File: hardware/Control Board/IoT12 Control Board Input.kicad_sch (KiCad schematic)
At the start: 28 parts, among them SW1 Rotary encoder EC11 Plum 15mm, U2 ADS1115IDGS, U3 INA826AID, U4 INA826AID

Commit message: Start of next iteration.
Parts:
- removed J1, J2: ~, TestPoint:TestPoint_THTPad_D2.0mm_Drill1.0mm, symbol Connector_Generic:Conn_01x01
- removed SW1: Rotary encoder EC11 Plum 15mm, Rotary_Encoder-fixed:RotaryEncoder_Alps_EC11E-Switch_Vertical_H20mm_CircularMountingHoles, symbol Device:RotaryEncoder_Switch
- added J6: JST B6B-XH-A, Connector_JST:JST_XH_B6B-XH-A_1x06_P2.50mm_Vertical, symbol Connector:Conn_01x06_Male
- NT1: footprint NetTie-extra:NetTie-2_SMD_Pad0.25mm -> NetTie-extra:NetTie-2_SMD_Pad0.5mm; now left out of the parts list
- R74: renamed from R80; value 1M -> 100k
- R75: renamed from R81; value 1M -> 100k
- U3, U4: footprint Package_SO:SOIC-8_3.9x4.9mm_P1.27mm -> Package_SO:MSOP-8_3x3mm_P0.65mm
- renumbered R50 to R47, R51 to R48
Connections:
- net GND: now also J6.5 (Pin_5)
- net NTC_IN: now reaches R48.2, R64.2
- net SHAKE_IN: now reaches R75.2
- net +3V3 renamed +3.3V
- net +3.3V: now also J6.6 (Pin_6)
- net AIN_COMP renamed SHAKE
- new net EXP_D5: J6.1 (Pin_1)
- new net EXP_D7: J6.2 (Pin_2)
- new net EXP_SCL: J6.3 (Pin_3)
- new net EXP_SDA: J6.4 (Pin_4)
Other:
- note added: "16b I2C ADC"
- note added: "Expansion I/O"
- note added: "Shake sensor"
- note removed: "External 16b I2C ADC"
- note removed: "NTC"
- note removed: "Shake"
- note removed: "Tilt switch sensor as shake sensor"
- note removed: "User input"
- company: (none) -> https://github.com/atoomnetmarc/IoT12
- title: IoT12-hardware input and sensors -> IoT12 Control Board
- moved on the sheet: C10, NT1, R48, R64, R74, R75

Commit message: Corrected footprint for INA826AID.
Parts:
- U3, U4: footprint Package_SO:MSOP-8_3x3mm_P0.65mm -> Package_SO-fixed:SOIC-8_5.23x5.23mm_P1.27mm
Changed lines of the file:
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@@
       (effects (font (size 1.27 1.27)) (justify left))
     )
-    (property "Footprint" "Package_SO:MSOP-8_3x3mm_P0.65mm" (id 2) (at 107.95 45.72 0)
+    (property "Footprint" "Package_SO-fixed:SOIC-8_5.23x5.23mm_P1.27mm" (id 2) (at 107.95 45.72 0)
       (effects (font (size 1.27 1.27)) hide)
     )
@@
       (effects (font (size 1.27 1.27)) (justify left))
     )
-    (property "Footprint" "Package_SO:MSOP-8_3x3mm_P0.65mm" (id 2) (at 236.22 45.72 0)
-      (effects (font (size 1.27 1.27)) hide)
-    )
+    (property "Footprint" "Package_SO-fixed:SOIC-8_5.23x5.23mm_P1.27mm" (id 2) (at 236.22 45.72 0)
+      (effects (font (size 1.27 1.27)) hide)
+    )

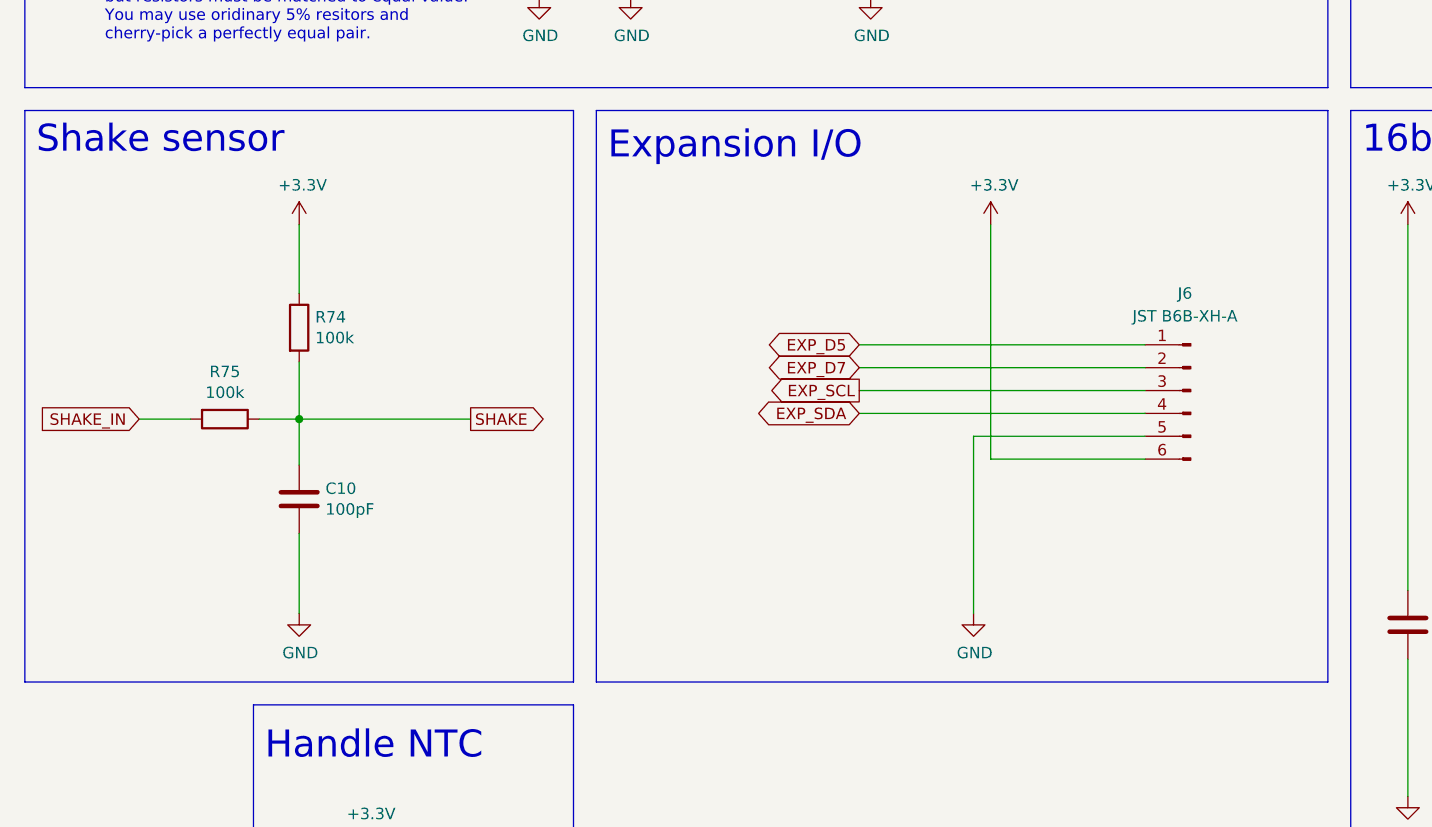
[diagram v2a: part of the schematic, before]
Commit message: Update Control Board project to Kicad 7.0.2
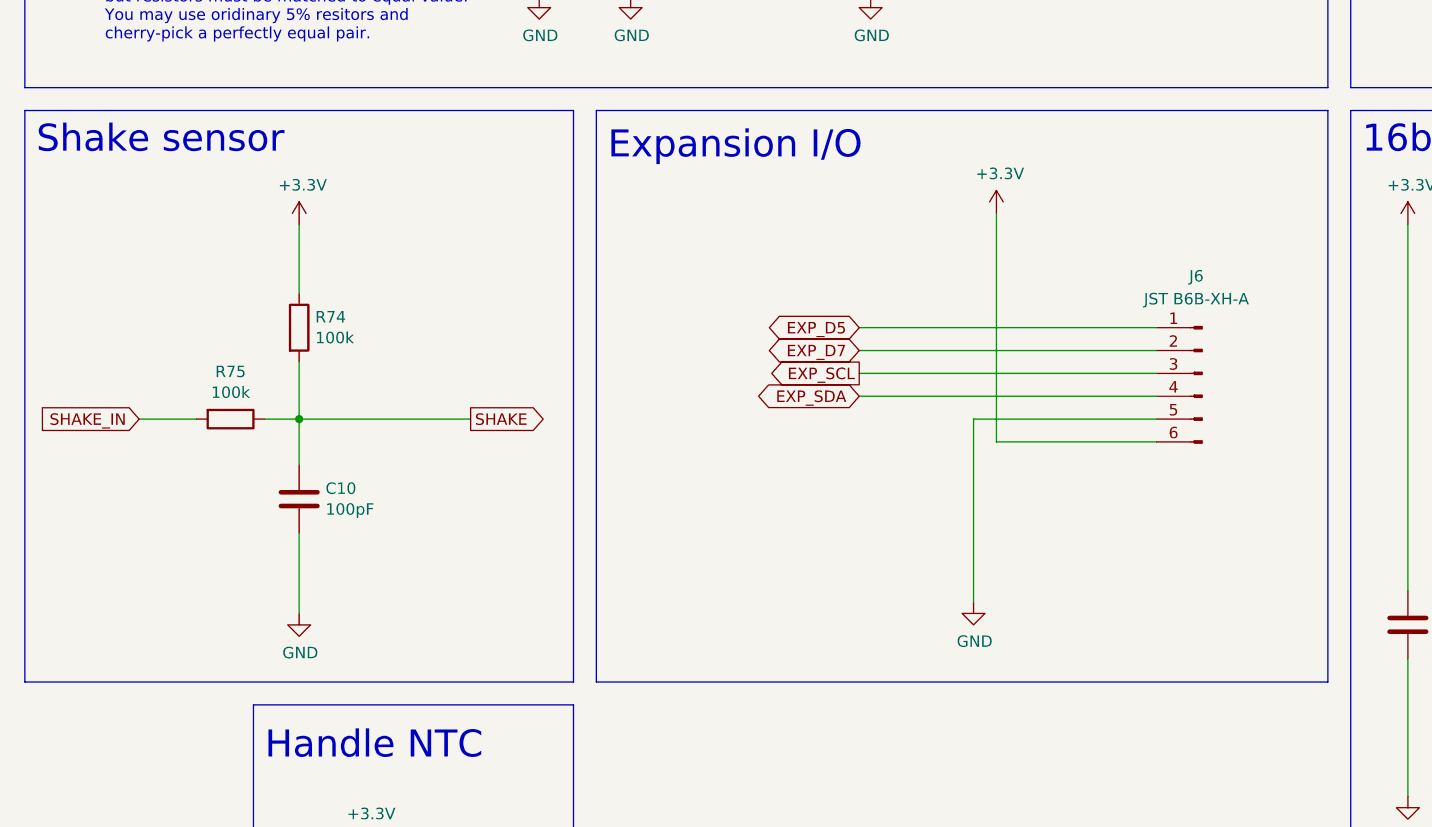
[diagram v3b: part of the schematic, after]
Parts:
- J6: symbol Connector:Conn_01x06_Male -> Connector:Conn_01x06_Pin
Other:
- moved on the sheet: J6, R75
